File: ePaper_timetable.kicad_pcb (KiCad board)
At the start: 2 copper layers, 43 parts, among them J1 26 pin FPC connector 0.5 mm p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, J3 Battery connector, Q1 BSS138, Q2 AO3401A, Q3 FS8205A, SW1 SW_Push, SW2 SW_Push, SW3 SW_Push, U1 Pico, U2 DW01A, U3 TP4056

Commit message: display 3d model added
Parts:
- added REF**: 7_5 inch display, 7_5 inch display model:7_5 inch display, B.Cu at (171.4, 63.5)
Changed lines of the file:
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@@
+    )
+  )
+  (footprint "7_5 inch display model:7_5 inch display" (layer "B.Cu")
+    (at 171.45 63.5 180)
+    (attr smd)
+    (fp_text reference "REF**" (at 1.27 0.5 unlocked) (layer "F.SilkS")
+        (effects (font (size 1 1) (thickness 0.1)))
+    )
+    (fp_text value "7_5 inch display" (at 1.27 -1 unlocked) (layer "F.Fab")
+        (effects (font (size 1 1) (thickness 0.15)))
+    )
+    (fp_text user "${REFERENCE}" (at 1.27 -2.5 unlocked) (layer "F.Fab")
+        (effects (font (size 1 1) (thickness 0.15)))
+    )
+    (model "${KIPRJMOD}/libraries/Waveshare display 3d models/Waveshare 7.5 E-ink (B) - Display Flat Mount.stp"
+      (offset (xyz 0 0 0))
+      (scale (xyz 1 1 1))
+      (rotate (xyz 0 0 0))
     )
   )

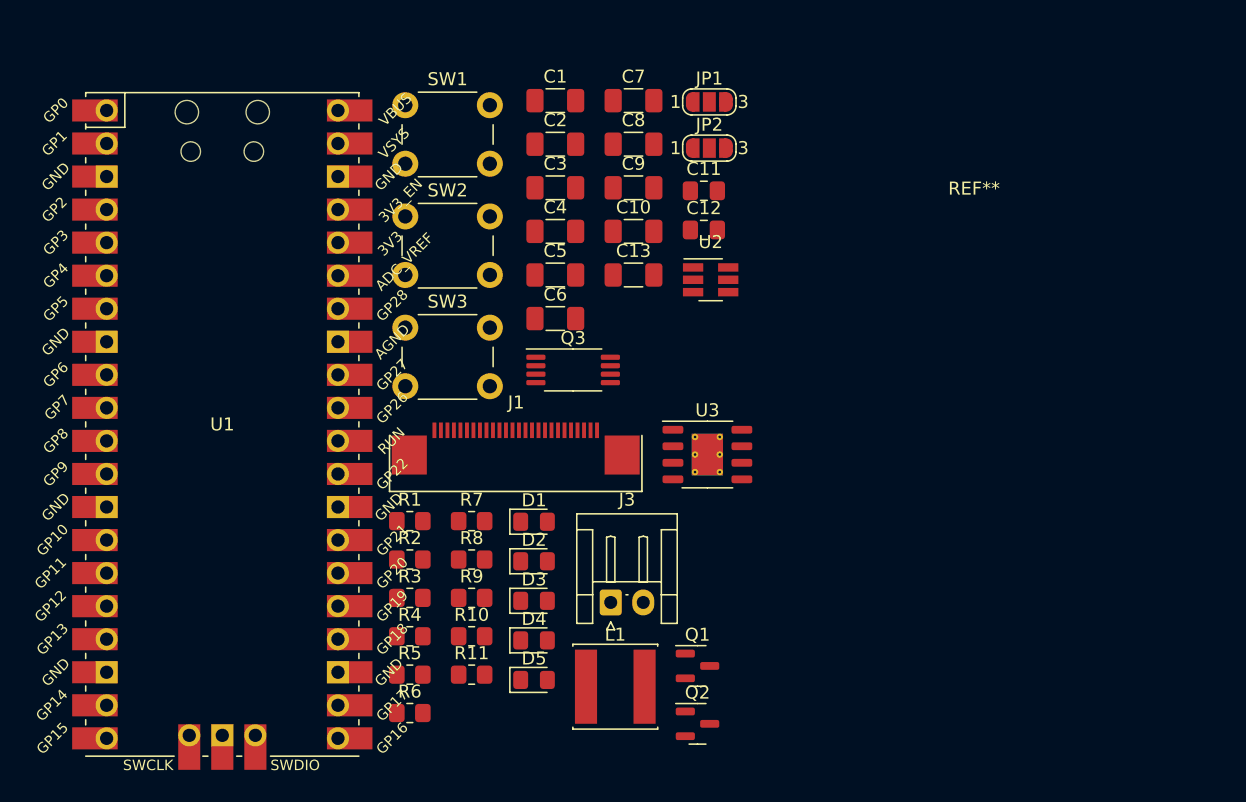
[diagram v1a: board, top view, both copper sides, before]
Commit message: fixed pcb - not saved previously
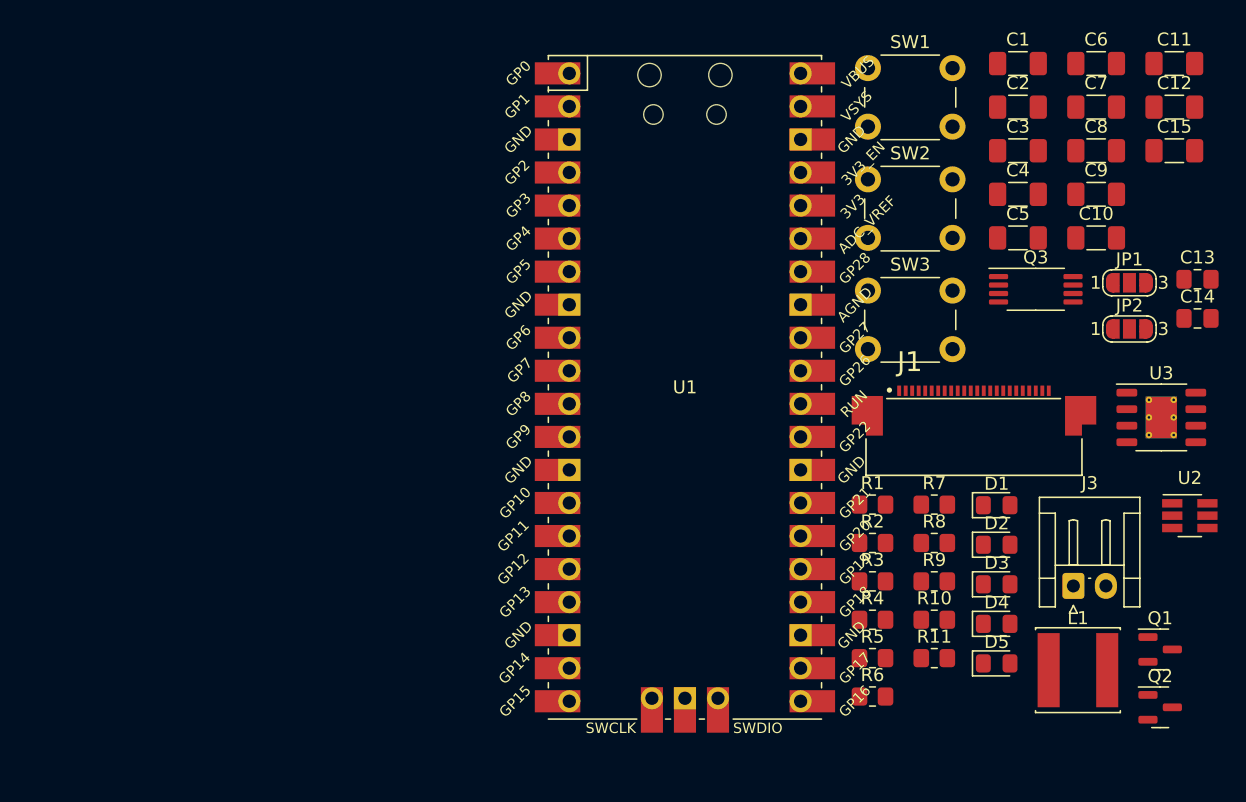
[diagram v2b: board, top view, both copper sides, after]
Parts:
- added C14: 100n, Capacitor_SMD:C_0805_2012Metric_Pad1.18x1.45mm_HandSolder, F.Cu at (187.4, 73.0)
- added C15: 10u, Capacitor_SMD:C_1206_3216Metric_Pad1.33x1.80mm_HandSolder, F.Cu at (185.6, 60.1)
- C10: value 1u/50V -> 1u
- C11: value 100n -> 1u; footprint Capacitor_SMD:C_0805_2012Metric_Pad1.18x1.45mm_HandSolder -> Capacitor_SMD:C_1206_3216Metric_Pad1.33x1.80mm_HandSolder
- C12: value 100n -> 1u/50V; footprint Capacitor_SMD:C_0805_2012Metric_Pad1.18x1.45mm_HandSolder -> Capacitor_SMD:C_1206_3216Metric_Pad1.33x1.80mm_HandSolder
- C13: value 10u -> 100n; footprint Capacitor_SMD:C_1206_3216Metric_Pad1.33x1.80mm_HandSolder -> Capacitor_SMD:C_0805_2012Metric_Pad1.18x1.45mm_HandSolder
- C6, C9: value 1u/10V -> 1u
- C8: value 1u -> 1u/10V
- J1: value 26 pin FPC connector 0.5 mm pitch -> 52435-2471; footprint FPC conn:68712614522 -> 52435-2471:MOLEX_52435-2471
- moved C6 46.0 mm to (179.6, 53.4)
- moved C13 43.4 mm to (187.4, 70.0)
- moved U2 41.1 mm to (186.8, 88.1)
- moved C11 37.5 mm to (185.6, 53.4)
- moved C12 37.4 mm to (185.6, 56.7)
- moved Q3 36.1 mm to (174.9, 70.7)
- moved U1 35.7 mm to (148.0, 78.3)
- moved C1 35.7 mm to (173.6, 53.4)
- moved C2 35.7 mm to (173.6, 56.7)
- moved C3 35.7 mm to (173.6, 60.1)
- moved C4 35.7 mm to (173.6, 63.4)
- moved C5 35.7 mm to (173.6, 66.8)
- moved SW1 35.7 mm to (162.0, 53.7)
- moved SW2 35.7 mm to (162.0, 62.3)
- moved SW3 35.7 mm to (162.0, 70.8)
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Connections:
- C10 pad 2: Net-(C10-Pad2) -> /VGL
- C11 pad 2: Net-(D4-A) -> Net-(C11-Pad2)
- C12 pad 1: /Battery- -> GND
- C12 pad 2: /DW01_{Vcc} -> Net-(C12-Pad2)
- C13 pad 2: /V_{battery} -> Net-(D4-A)
- C4 pad 2: /VGH -> Net-(C4-Pad2)
- C6 pad 2: /3.3V -> /VGH
- C8 pad 2: /VGL -> /3.3V
- J1 pad 18: Net-(C9-Pad2) -> Net-(C11-Pad2)
- J1 pad 19: unconnected-(J1-Pad19) -> Net-(C4-Pad2)
- J1 pad 22: Net-(C7-Pad2) -> Net-(C9-Pad2)
- J1 pad 24: Net-(C10-Pad2) -> Net-(C12-Pad2)
- J1 pad 4: unconnected-(J1-Pad4) -> Net-(C5-Pad2)
- J1 pad 5: Net-(C5-Pad2) -> Net-(C7-Pad2)

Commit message: update sch and pcb
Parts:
- removed REF**: 7_5 inch display, 7_5 inch display model:7_5 inch display
- added A1: RaspberryPi-Pico(W), MCU_RPi_Pico:Raspberry_Pi_Pico_W_SMT, F.Cu at (104.3, 56.8)
- added C16: 10u, Capacitor_SMD:C_0805_2012Metric_Pad1.18x1.45mm_HandSolder, F.Cu at (137.3, 89.3)
- added F1: Polyfuse, Fuse:Fuse_1812_4532Metric_Pad1.30x3.40mm_HandSolder, F.Cu at (116.4, 110.5)
- added J2: 52435-2471, 52435-2471:MOLEX_52435-2471, F.Cu at (149.8, 79.0)
- added J4: Charging input - 5V, Connector_Phoenix_MC:PhoenixContact_MC_1,5_2-G-3.81_1x02_P3.81mm_Horizontal, F.Cu at (129.0, 99.9)
- added J5: Conn_01x03_Socket, Connector_PinSocket_2.54mm:PinSocket_1x03_P2.54mm_Vertical, F.Cu at (146.6, 101.2)
- added J6: Conn_01x03_Socket, Connector_PinSocket_2.54mm:PinSocket_1x03_P2.54mm_Vertical, F.Cu at (151.2, 101.2)
- added J7: Conn_01x04_Socket, Connector_PinSocket_2.54mm:PinSocket_1x04_P2.54mm_Vertical, F.Cu at (157.3, 65.4)
- added J8: Battery connector, Connector_PinSocket_2.54mm:PinSocket_1x02_P2.54mm_Vertical, F.Cu at (122.4, 110.3)
- added J9: Conn_01x01_Pin, Connector_Wire:SolderWirePad_1x01_SMD_1x2mm, F.Cu at (160.5, 110.7)
- added Q4: BSS138, Package_TO_SOT_SMD:SOT-23, F.Cu at (152.5, 74.2)
- added R12: 10k, Resistor_SMD:R_0805_2012Metric_Pad1.20x1.40mm_HandSolder, F.Cu at (142.9, 63.4)
- added R13: 100R, Resistor_SMD:R_0805_2012Metric_Pad1.20x1.40mm_HandSolder, F.Cu at (142.9, 66.3)
- added R14: 100R, Resistor_SMD:R_0805_2012Metric_Pad1.20x1.40mm_HandSolder, F.Cu at (142.9, 69.3)
- added R15: 10k, Resistor_SMD:R_0805_2012Metric_Pad1.20x1.40mm_HandSolder, F.Cu at (142.9, 72.2)
- added R16: 0R, Resistor_SMD:R_1206_3216Metric_Pad1.30x1.75mm_HandSolder, F.Cu at (109.8, 112.9)
- added R17: 1.2k, Resistor_SMD:R_0805_2012Metric_Pad1.20x1.40mm_HandSolder, F.Cu at (147.7, 54.5)
- added R18: 1k, Resistor_SMD:R_0805_2012Metric_Pad1.20x1.40mm_HandSolder, F.Cu at (147.7, 57.5)
- added R19: 100, Resistor_SMD:R_0805_2012Metric_Pad1.20x1.40mm_HandSolder, F.Cu at (147.7, 60.4)
- added R20: 1.2k, Resistor_SMD:R_0805_2012Metric_Pad1.20x1.40mm_HandSolder, F.Cu at (147.7, 63.4)
- added R21: 1.2k, Resistor_SMD:R_0805_2012Metric_Pad1.20x1.40mm_HandSolder, F.Cu at (147.7, 66.3)
- added R22: 200k, Resistor_SMD:R_0805_2012Metric_Pad1.20x1.40mm_HandSolder, F.Cu at (147.7, 69.3)
- added R23: 100k, Resistor_SMD:R_0805_2012Metric_Pad1.20x1.40mm_HandSolder, F.Cu at (147.7, 72.2)
- added SW4: SW_Push, Button_Switch_THT:SW_PUSH_6mm_H7.3mm, F.Cu at (127.3, 72.2)
- added SW5: SW_Push, Button_Switch_SMD:SW_Tactile_SPST_NO_Straight_CK_PTS636Sx25SMTRLFS, F.Cu at (146.0, 95.9)
- C1, C10, C11, C12, C2, C3, C4, C5, C6, C7, C8, C9: footprint Capacitor_SMD:C_1206_3216Metric_Pad1.33x1.80mm_HandSolder -> Capacitor_SMD:C_0805_2012Metric_Pad1.18x1.45mm_HandSolder
- C15: value 10u -> 1n; footprint Capacitor_SMD:C_1206_3216Metric_Pad1.33x1.80mm_HandSolder -> Capacitor_SMD:C_0805_2012Metric_Pad1.18x1.45mm_HandSolder
- D1, D2, D3: footprint Diode_SMD:D_0805_2012Metric_Pad1.15x1.40mm_HandSolder -> Diode_SMD:D_SOD-123
- J1: value 52435-2471 -> USB_C_Receptacle_USB2.0; footprint 52435-2471:MOLEX_52435-2471 -> Connector_USB:USB_C_Receptacle_GCT_USB4105-xx-A_16P_TopMnt_Horizontal
- J3: value Battery connector -> Conn_01x03_Socket; footprint Connector_JST:JST_EH_S2B-EH_1x02_P2.50mm_Horizontal -> Connector_PinSocket_2.54mm:PinSocket_1x03_P2.54mm_Vertical
- R10, R11: value 1.2k -> 100R
- R4, R5: value 1k -> 5k1
- R6: value 1k -> 0R; footprint Resistor_SMD:R_0805_2012Metric_Pad1.20x1.40mm_HandSolder -> Resistor_SMD:R_1206_3216Metric_Pad1.30x1.75mm_HandSolder
- R7: value 1.2k -> 1k
- R9: value 100 -> 1k
- SW1: footprint Button_Switch_THT:SW_PUSH_6mm_H7.3mm -> Button_Switch_SMD:SW_Tactile_SPST_NO_Straight_CK_PTS636Sx25SMTRLFS
- U1: value Pico -> USBLC6-2SC6; footprint MCU_RaspberryPi_and_Boards:RPi_Pico_SMD_TH -> Package_TO_SOT_SMD:SOT-23-6
- U3: footprint Package_SO:HTSOP-8-1EP_3.9x4.9mm_P1.27mm_EP2.4x3.2mm_ThermalVias -> Package_SO:HTSOP-8-1EP_3.9x4.9mm_P1.27mm_EP2.4x3.2mm
- moved JP1 87.6 mm to (104.0, 109.8)
- moved JP2 87.6 mm to (104.0, 113.3)
- moved C6 66.7 mm to (127.7, 95.3)
- moved C11 65.8 mm to (132.5, 92.3)
- moved C12 65.6 mm to (132.5, 95.3)
- moved Q3 60.7 mm to (129.6, 111.2)
- moved C15 54.9 mm to (137.3, 86.2)
- moved R6 53.2 mm to (109.8, 109.6)
- moved C1 53.2 mm to (127.7, 80.2)
- moved C2 53.0 mm to (127.7, 83.2)
- moved C3 52.8 mm to (127.7, 86.2)
- moved C4 52.6 mm to (127.7, 89.3)
- moved C7 52.6 mm to (132.5, 80.2)
- moved C5 52.5 mm to (127.7, 92.3)
- moved C8 52.5 mm to (132.5, 83.2)
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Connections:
- C1 pad 2: /3.3V -> +3V3
- C13 pad 2: Net-(D4-A) -> +5V
- C14 pad 1: /Battery- -> -BATT
- C15 pad 2: /V_{battery} -> Net-(Q4-D)
- C8 pad 2: /3.3V -> +3V3
- D4 pad 2: Net-(D4-A) -> +5V
- D5 pad 2: Net-(D4-A) -> +5V
- J3 pad 1: /V_{battery} -> Net-(J3-Pin_1)
- J3 pad 2: /Battery- -> GND
- JP2 pad 1: /3.3V -> +3V3
- L1 pad 1: /3.3V -> +3V3
- Q2 pad 1: Net-(Q2-G) -> +5V
- Q2 pad 2: Net-(Q2-S) -> Net-(A1-VSYS)
- Q2 pad 3: /V_{battery} -> +BATT
- Q3 pad 6: /Battery- -> -BATT
- Q3 pad 7: /Battery- -> -BATT
- R10 pad 1: Net-(D4-K) -> Net-(J3-Pin_1)
- R10 pad 2: Net-(U3-~{STDBY}) -> /SWCLK
- R11 pad 1: Net-(D5-K) -> Net-(J3-Pin_3)
- R11 pad 2: Net-(U3-~{CHRG}) -> /SWDIO
- R4 pad 1: /3.3V -> Net-(J1-CC1)
- R4 pad 2: /SW1 -> GND
- R5 pad 1: /3.3V -> Net-(J1-CC2)
- R5 pad 2: /SW2 -> GND
- R6 pad 1: /3.3V -> Net-(U1-VBUS)
- R6 pad 2: /SW3 -> +5V
- R7 pad 1: Net-(U3-PROG) -> +3V3
- R7 pad 2: GND -> /SW1
- R8 pad 1: Net-(U2-CS) -> +3V3
- R8 pad 2: GND -> /SW2
- R9 pad 1: /DW01_{Vcc} -> +3V3
- R9 pad 2: /V_{battery} -> /SW3
- SW1 pad 1: GND -> Net-(A1-RUN)
- SW1 pad 2: /SW1 -> GND
- SW2 pad 2: /SW2 -> /SW1
- SW3 pad 2: /SW3 -> /SW2
- U1 pad 1: /EPD_RST' -> Net-(J1-D+-PadA6)
- U1 pad 2: unconnected-(U1-GPIO1-Pad2) -> GND
- U1 pad 3: GND -> /USB_DP
- U1 pad 4: unconnected-(U1-GPIO2-Pad4) -> /USB_DM
- U1 pad 5: unconnected-(U1-GPIO3-Pad5) -> Net-(U1-VBUS)
- U1 pad 6: unconnected-(U1-GPIO4-Pad6) -> Net-(J1-D--PadA7)
- U2 pad 6: /Battery- -> -BATT
- U3 pad 4: Net-(D4-A) -> +5V
- U3 pad 5: /V_{battery} -> +BATT
- U3 pad 6: Net-(U3-~{STDBY}) -> /BAT_STDBY
- U3 pad 7: Net-(U3-~{CHRG}) -> /BAT_CHRG
- U3 pad 8: Net-(D4-A) -> +5V
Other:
- board outline added: 91.6 x 85.5 mm
